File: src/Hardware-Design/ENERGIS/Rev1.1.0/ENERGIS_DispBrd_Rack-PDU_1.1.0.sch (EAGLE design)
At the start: 78 parts, among them CON1 DNI, CON2 AFC11-S20ICC-00, IC1 MCP23017T-E/ML, IC2 MCP23017T-E/ML, T1 DNI

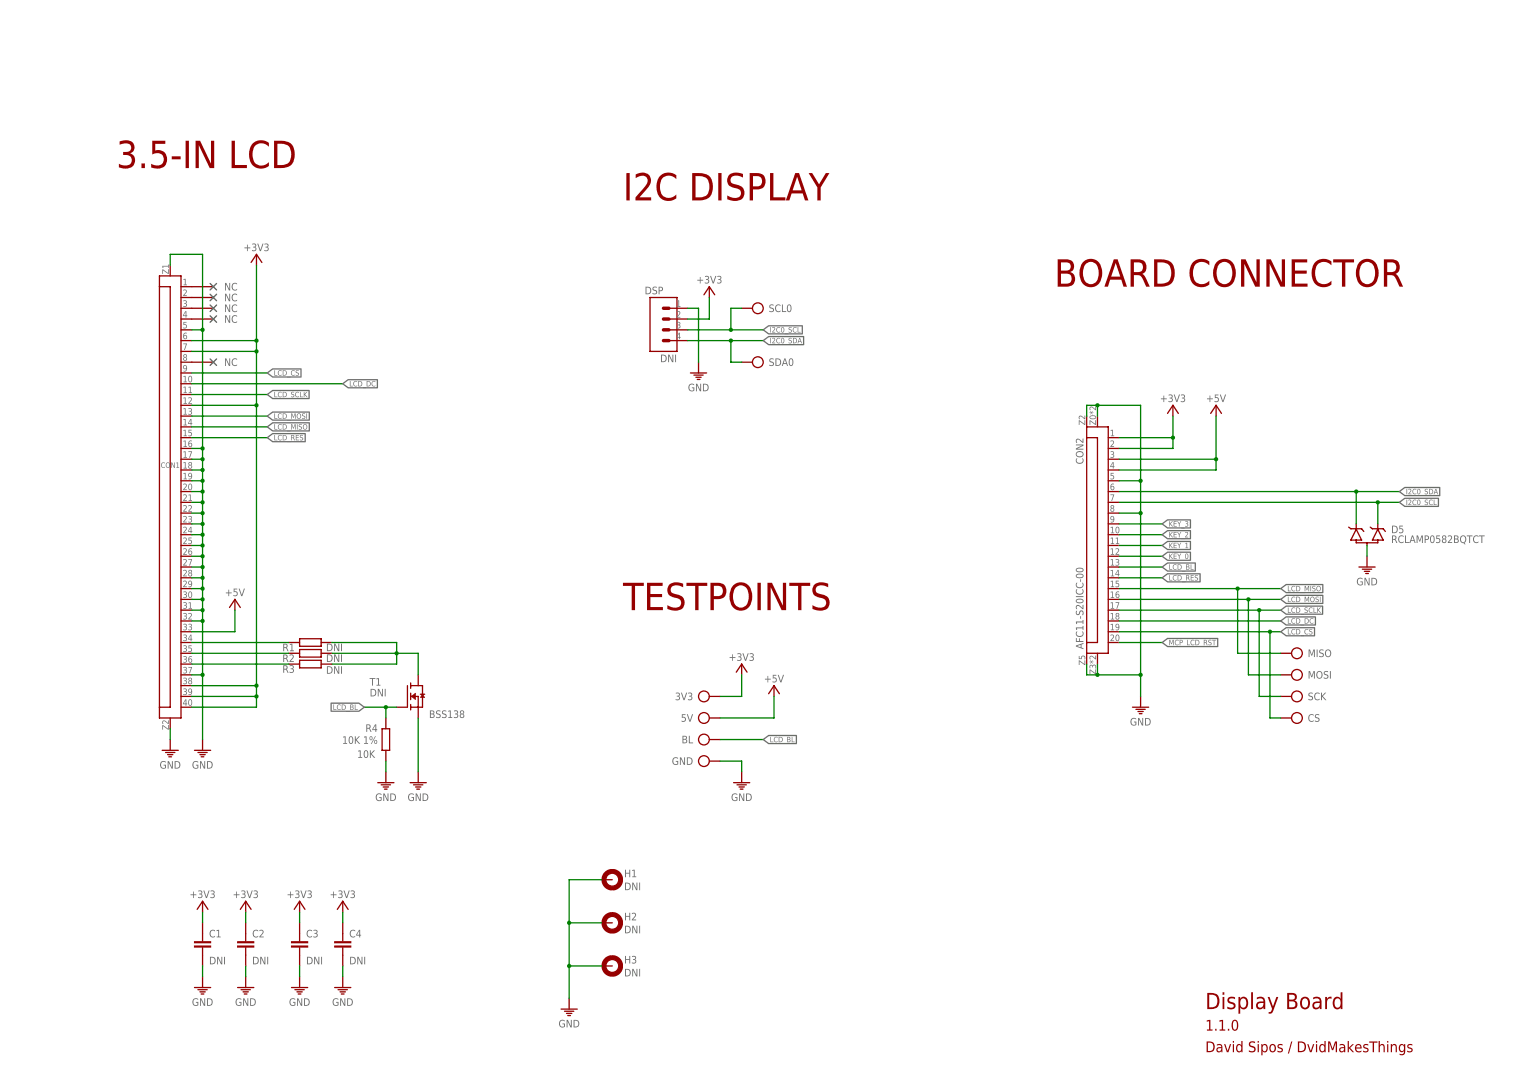
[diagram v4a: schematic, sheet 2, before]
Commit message: clear documentation, software bugfix
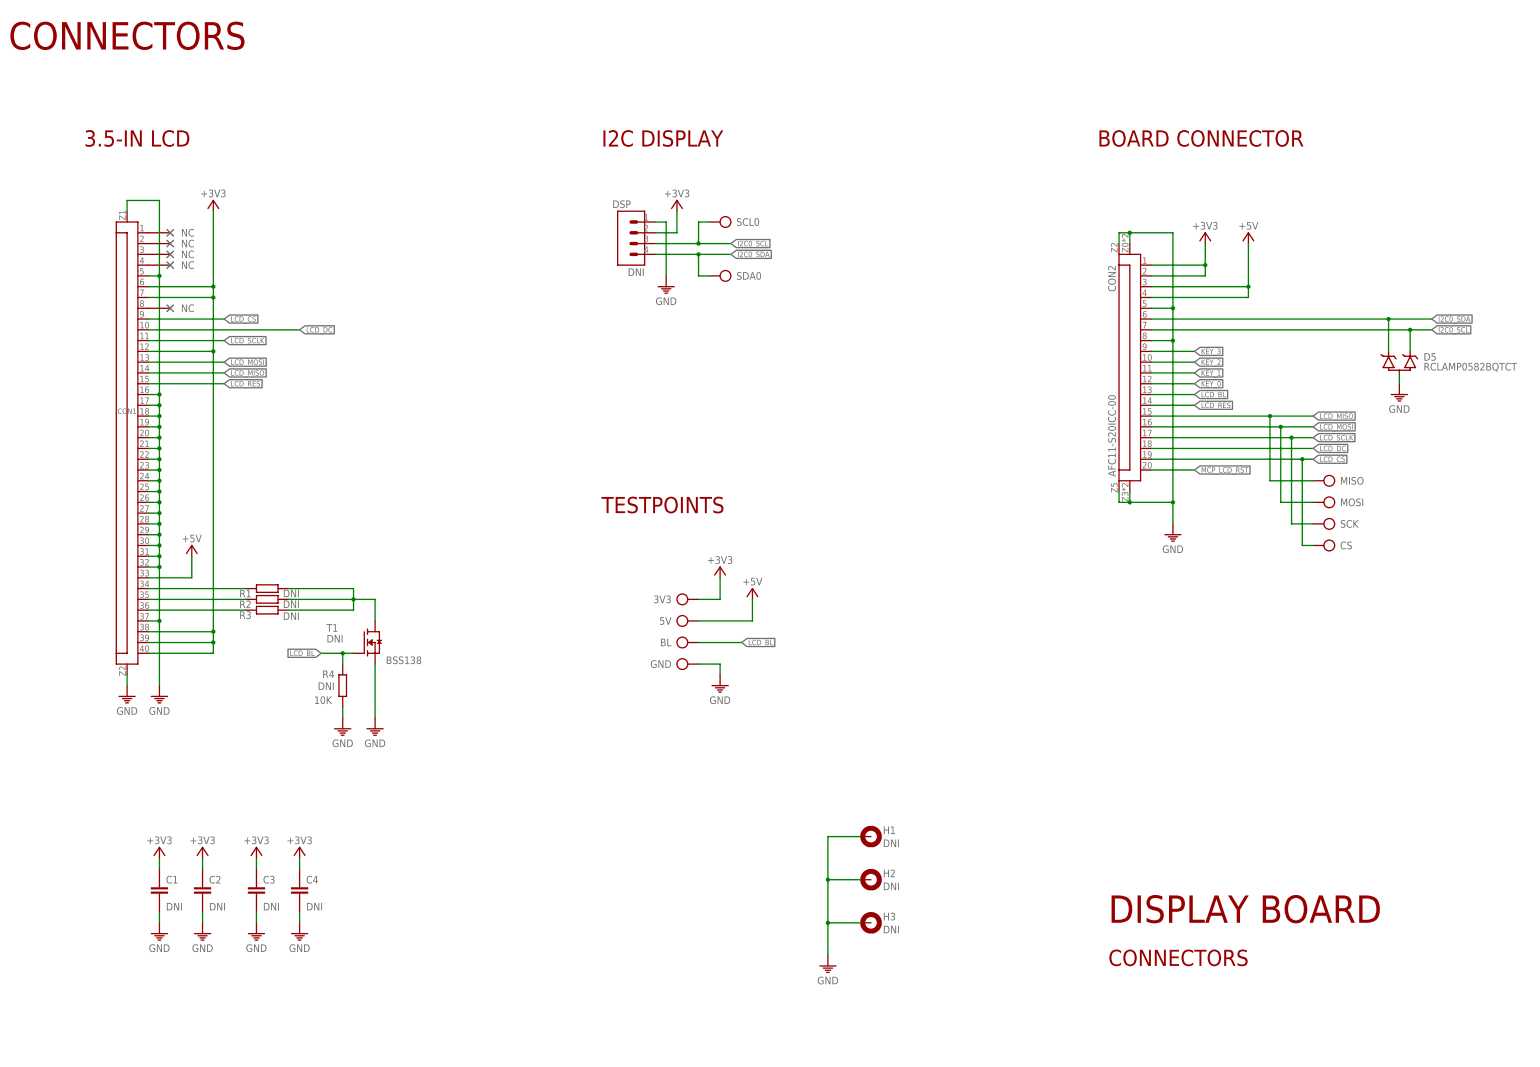
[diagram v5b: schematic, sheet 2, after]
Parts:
- R4: value 10K 1% -> DNI
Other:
- note added: "CONNECTORS"
- note added: "DISPLAY BOARD"
- note added: "DISPLAY LEDS"
- note added: "IO DRIVERS"
- note added: "SELECTION LEDS"
- note removed: "David Sipos / DvidMakesThings"
- note removed: "Display Board"
- note removed: "IO DRIVER"
- moved on the sheet: 3V3, 5V, BL, C1, C2, C3, C4, CON1, CON2, CS, D5, DSP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
